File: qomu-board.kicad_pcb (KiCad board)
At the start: 6 copper layers, 28.1 x 10.7 mm, 67 parts, among them IC1 EOS-S3, J1 FTSH-105-01-L-DV-K, J2 825437-4, J3 MC-HVT1-S02-G, Q1 RV1C002UN, Q2 RV1C002UN, Q3 RV1C002UN, SW2 Captouch Pads, U1 MIC5504-3.3YMT, U10 UHD1110-FKA, U2 MIC5504-3.3YMT, U4 GD25Q16CEIGR, U5 MC3635, U9 USB-B

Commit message: Update Kicad design file
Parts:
- added N3: ql_logo, qomu-board-footprints:Ql_logo_mid_9mm, F.Cu at (21.4, 22.3)
- N2: footprint qomu-board-footprints:antmicro-logo_midlayer -> qomu-board-footprints:antmicro-logo_midlayer_4mm
- U4: value GD25Q16CEIGR -> GD25Q16C; footprint qomu-board:GD25Q16CEIGR -> qomu-board-footprints:GD25Q16CEIGR
- moved N2 14.7 mm to (37.1, 21.6), turned to 0 degrees
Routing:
- net GND: track 53.4 -> 51.3 mm
- net +3V3: track 57.9 -> 58.5 mm
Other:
- board size 28.1 x 10.7 mm -> 28.1 x 10.6 mm
- board text added: "qomu"
- board text added: "rev.1.1"
- board text added: "v.1.1"
- board text removed: "Qomu"
- board text removed: "rev.1.0"

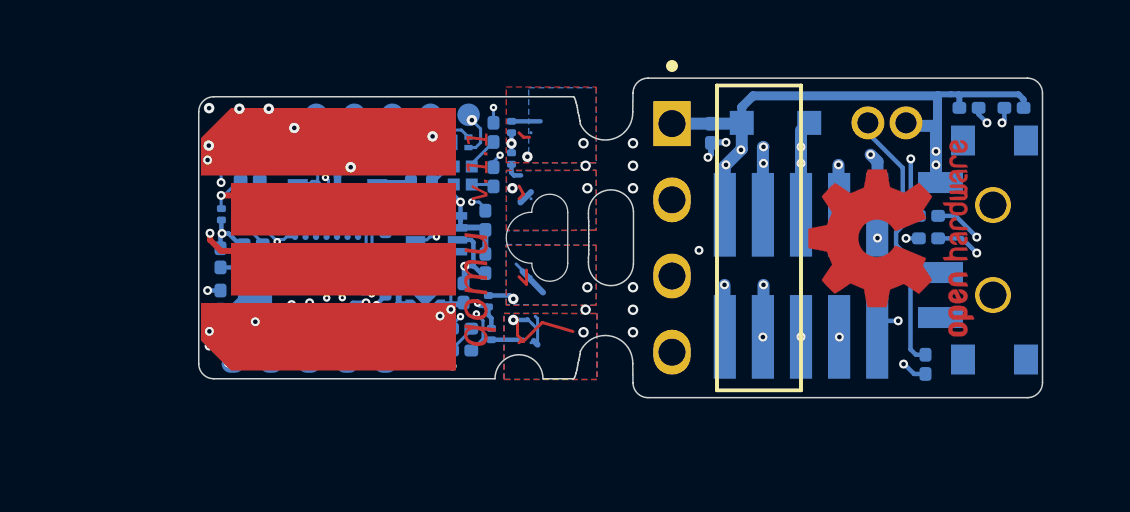
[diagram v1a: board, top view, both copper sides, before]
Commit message: Schematic Update: 1. Remove accel sensor and related passive components 2. Add QL to title Layout Update: 1. Remove accel sensor and related passive components 2. Remove stranded nets: I2C SCL, I2C SDA, IMU_INT, 3,3V, GND
Remains: check stranded via for 3.3V and GND
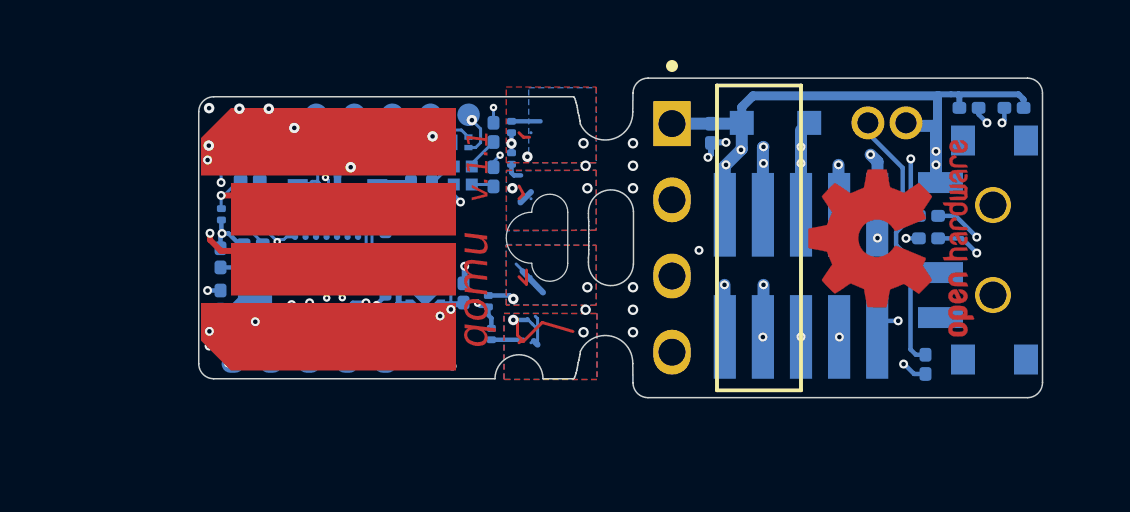
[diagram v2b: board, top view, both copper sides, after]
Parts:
- removed C4: 100n, qomu-board-footprints:C_0201_0603Metric
- removed R3, R4, R8: 4k7, qomu-board-footprints:R_0201_0603Metric
- removed U5: MC3635, qomu-board:MC3635
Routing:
- net /I2C_SDA: track 8.33 -> 0.00 mm, vias 3 -> 0
- net /ACC_INT: track 6.43 -> 0.00 mm, vias 3 -> 0
- net /I2C_SCL: track 5.84 -> 0.00 mm, vias 3 -> 0
- net +3V3: track 58.5 -> 53.6 mm
- net GND: track 51.3 -> 48.0 mm

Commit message: pcb: first attempt at new component placement
There's still a huge ratsnest, but component placement should roughly be
finalized.

Signed-off-by: Sean Cross <sean@xobs.io>
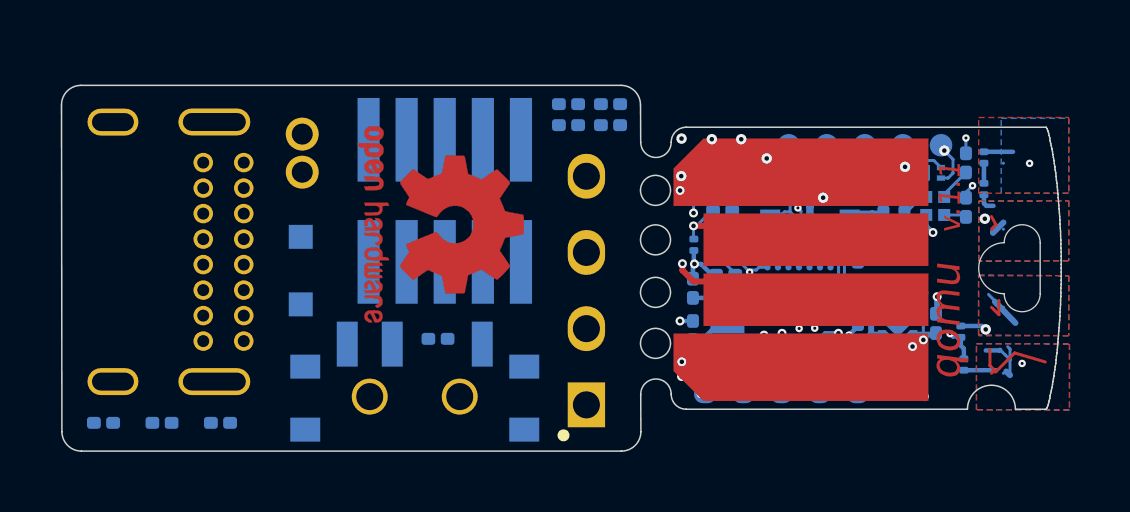
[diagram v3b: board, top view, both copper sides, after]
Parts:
- added J4: USB-C, qomu-board-footprints:USB4085-GF-A, B.Cu at (14.5, 22.3)
- added R3: 5.1k, 1%, 0201, qomu-board-footprints:R_0201_0603Metric, B.Cu at (15.8, 28.0)
- added R4: 5.1k, 1%, 0201, qomu-board-footprints:R_0201_0603Metric, B.Cu at (13.8, 28.0)
- C1, C2, C7, C9: value 2u2/10V -> 2u2, 10V, X5R, 0201
- C10, C11, C12, C3, C5, C6, C8: value 100n -> 100n, 6.3V, X5R, 0201
- C13, C14: value 8p -> 8p, 25V, NP0, 0201
- R1, R13, R15, R2, R5, R6: value 10k -> 10k, 1%, 0201
- R10, R7: value 0R -> 0R, 0201
- R11, R12: value 22R -> 22R, 1%, 0201
- R16, R17: value 100R -> 100R, 1%, 0201
- R18: value 220R -> 220R, 1%, 0201
- R9: value 1k5 -> 1k5, 1%, 0201
- U4: value GD25Q16C -> GD25Q16CEIGR
- moved R6 23.6 mm to (17.8, 28.0), turned to 180 degrees
- moved N2 22.5 mm to (14.7, 23.0)
- moved J3 20.1 mm to (20.5, 18.3), turned to 270 degrees
- moved S1 19.9 mm to (24.2, 27.1), turned to 180 degrees
- moved D8 16.6 mm to (20.4, 22.9), turned to 270 degrees
- moved C1 15.8 mm to (34.2, 25.9)
- moved C7 15.8 mm to (38.6, 25.5)
- moved R2 15.8 mm to (38.6, 26.2)
- moved TP9 15.8 mm to (37.7, 27.0)
- moved U4 15.8 mm to (37.4, 20.8)
- moved XTAL1 15.8 mm to (34.6, 24.3)
- moved C3 15.8 mm to (34.6, 23.0)
- moved C6 15.8 mm to (37.2, 26.2)
- moved C9 15.8 mm to (37.2, 25.5)
- moved D1 15.8 mm to (43.2, 19.1)
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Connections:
- IC1 pad A2: Net-(IC1-PadA2) -> (no net)
- IC1 pad A3: Net-(IC1-PadA3) -> (no net)
- IC1 pad A7: /I2C_SCL -> (no net)
- IC1 pad B2: Net-(IC1-PadB2) -> (no net)
- IC1 pad B7: /I2C_SDA -> (no net)
- IC1 pad C7: /ACC_INT -> (no net)
- IC1 pad D1: Net-(IC1-PadD1) -> (no net)
- J1 pad 7: Net-(J1-Pad7) -> (no net)
- S1 pad 3: Net-(S1-Pad3) -> (no net)
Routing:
- net /SWD_IO: track 31.9 -> 0.00 mm, vias 3 -> 1
- net /RST_N: track 32.4 -> 1.48 mm, vias 6 -> 2
- net +3V3: track 53.6 -> 27.9 mm, vias 28 -> 18
- net /UART_RX: track 26.0 -> 1.01 mm, vias 2 -> 1
- net /C1: track 27.9 -> 4.36 mm, vias 6 -> 4
- net /UART_TX: track 24.6 -> 3.16 mm, vias 3 -> 1
- net /SWD_CLK: track 31.1 -> 13.1 mm, vias 4 -> 7
- net GND: track 48.0 -> 30.7 mm, vias 57 -> 44
- net /LED_G: track 13.3 -> 0.49 mm, vias 8 -> 2
- net Net-(J3-Pad2): track 10.1 -> 0.00 mm
- net /TOUCH_4: track 12.0 -> 2.41 mm
- net Net-(J1-Pad6): track 8.82 -> 0.00 mm, vias 2 -> 0
- net /TOUCH_1: track 14.4 -> 6.18 mm
- net /R_USB_N: track 3.39 -> 11.5 mm, vias 2 -> 4
- net Net-(J1-Pad8): track 7.24 -> 0.00 mm, vias 2 -> 0
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- removed copper zone on In2.Cu, net GND
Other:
- board size 28.1 x 10.6 mm -> 33.3 x 12.2 mm
- board text removed: "1"

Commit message: pcb: re-layout board with new design rules
This lays out the board according to the design rules set forth by the
factory.
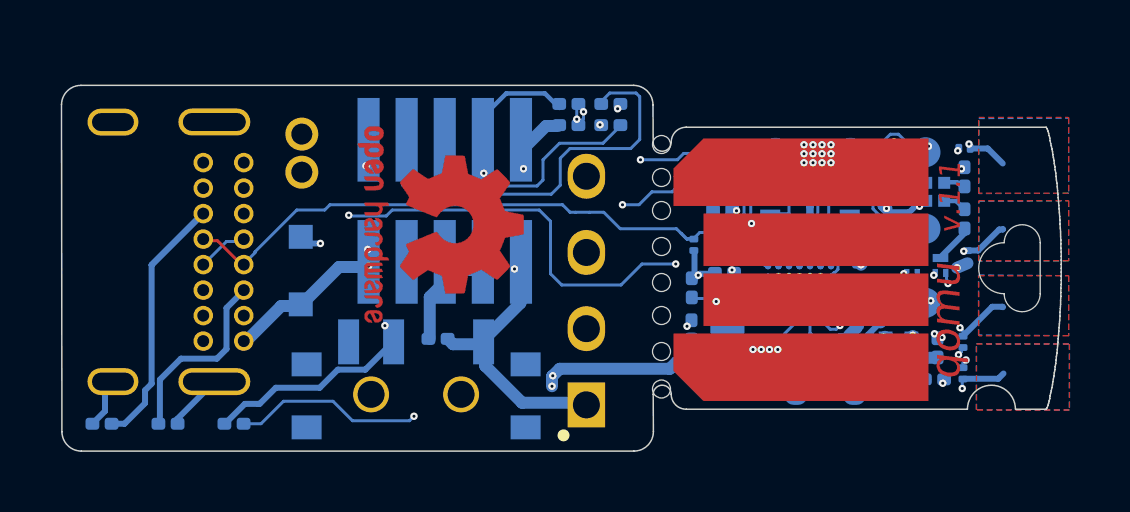
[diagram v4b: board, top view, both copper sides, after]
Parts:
- removed the IC1 at (37.0, 23.7)
- removed TP10, TP2: TP_SMD_0_75MM, qomu-board-footprints:Testpoint_smd_0_75_0_6mm
- removed TP8: TP_SMD_0_75MM, qomu-board-footprints:Testpoint_smd_0_75mm
- added IC1 (x2): EOS-S3, qomu-board:42-WLCSP, B.Cu at (37.0, 23.6)
- added REF**: Castellated_Via, qomu-board-footprints:Castellated_Via, F.Cu at (32.5, 21.6)
- added REF**: Castellated_Via, qomu-board-footprints:Castellated_Via, F.Cu at (32.5, 20.5)
- added REF**: Castellated_Via, qomu-board-footprints:Castellated_Via, F.Cu at (32.5, 22.7)
- added REF**: Castellated_Via, qomu-board-footprints:Castellated_Via, F.Cu at (32.5, 25.1)
- added REF**: Castellated_Via, qomu-board-footprints:Castellated_Via, F.Cu at (32.5, 23.9)
- added REF**: Castellated_Via, qomu-board-footprints:Castellated_Via, F.Cu at (32.5, 26.2)
- added REF**: Castellated_Via, qomu-board-footprints:Castellated_Via, F.Cu at (32.5, 27.4)
- added REF**: Castellated_Via, qomu-board-footprints:Castellated_Via, F.Cu at (32.5, 28.6)
- TP1: footprint qomu-board-footprints:Testpoint_smd_0_75_0_6mm -> qomu-board-footprints:Testpoint_pad_1mm
- TP4, TP5, TP6, TP7: footprint qomu-board-footprints:Testpoint_smd_0_75mm -> qomu-board-footprints:Testpoint_pad_1mm
- moved Q1 8.59 mm to (41.8, 22.8), turned to 90 degrees
- moved TP1 7.93 mm to (41.2, 24.0)
- moved Q2 6.89 mm to (40.8, 22.8), turned to 90 degrees
- moved N3 3.78 mm to (25.2, 22.5)
- moved TP6 3.48 mm to (41.2, 21.5)
- moved D3 2.31 mm to (42.6, 22.4), turned to 270 degrees
- moved R4 2.15 mm to (16.0, 28.0)
- moved R3 2.00 mm to (13.8, 28.0), turned to 0 degrees
- moved Q3 1.68 mm to (40.0, 19.0)
- moved R5 1.44 mm to (41.5, 26.5), turned to 0 degrees
- moved TP9 1.16 mm to (38.9, 27.0)
- moved TP5 0.85 mm to (38.8, 19.0)
- moved C2 0.82 mm to (41.6, 25.5)
- moved TP4 0.80 mm to (41.2, 18.9)
- moved N2 0.75 mm to (14.6, 22.3)
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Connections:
- J4 pad P2: (no net) -> GND
- J4 pad P3: (no net) -> GND
- J4 pad P4: (no net) -> GND
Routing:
- net GND: track 30.7 -> 133.5 mm, vias 44 -> 77
- net +3V3: track 27.9 -> 86.7 mm, vias 18 -> 36
- net +VBUS: track 5.40 -> 50.0 mm, vias 3 -> 27
- net /RST_N: track 1.48 -> 37.2 mm, vias 2 -> 5
- net /USB_P: track 6.28 -> 40.0 mm, vias 1 -> 3
- net /UART_TX: track 3.16 -> 25.8 mm, vias 1 -> 4
- net /C1: track 4.36 -> 24.9 mm, vias 4 -> 6
- net /UART_RX: track 1.01 -> 19.6 mm, vias 1 -> 4
- net /SWD_IO: track 0.00 -> 17.9 mm, vias 1 -> 2
- net /USB_N: track 8.19 -> 25.5 mm, vias 2 -> 4
- net /E1: track 15.0 -> 0.00 mm, vias 4 -> 0
- net Net-(J3-Pad2): track 0.00 -> 12.9 mm, vias 0 -> 1
- net Net-(J1-Pad8): track 0.00 -> 12.6 mm
- net /F2: track 11.7 -> 0.00 mm, vias 2 -> 0
- net /TOUCH_4: track 2.41 -> 13.6 mm, vias 4 -> 6
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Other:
- outline, holes or cut-outs redrawn
- board text added: "In2.Cu: 3.3V"
- board text added: "In3.Cu: GND Plane"

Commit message: pcb: fix routing and drc errors
This fixes all unconnected nets and DRC warnings/errors, and is ready
for fabrication.

Signed-off-by: Sean Cross <sean@xobs.io>
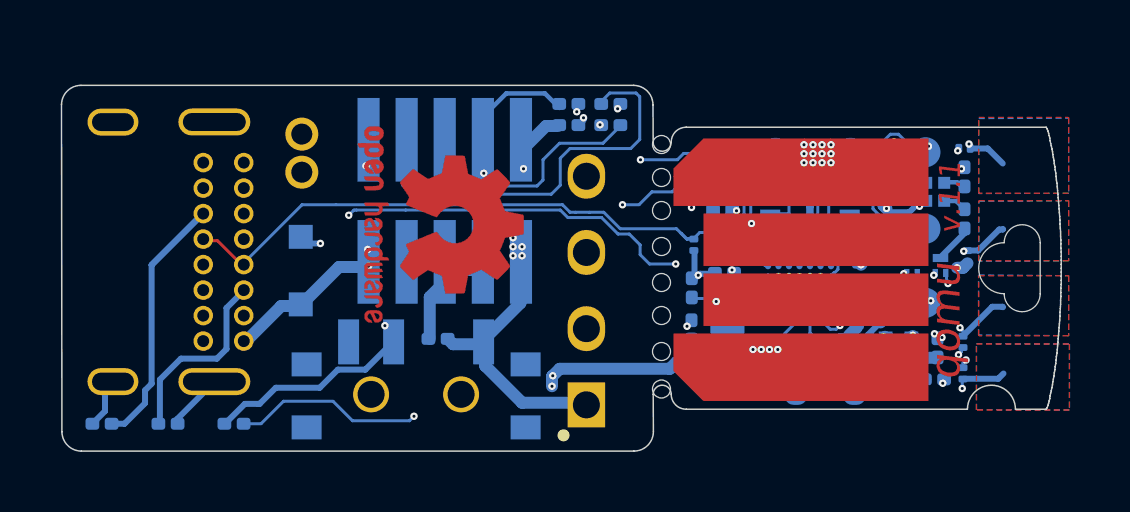
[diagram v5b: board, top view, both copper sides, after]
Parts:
- removed the IC1 at (37.0, 23.6)
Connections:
- IC1 pad A2: Net-(IC1-PadA2) -> (no net)
- IC1 pad A3: Net-(IC1-PadA3) -> (no net)
- IC1 pad B2: Net-(IC1-PadB2) -> (no net)
- IC1 pad B7: Net-(IC1-PadB7) -> (no net)
- IC1 pad C7: Net-(IC1-PadC7) -> (no net)
- IC1 pad D3: Net-(IC1-PadD3) -> (no net)
- IC1 pad E1: Net-(IC1-PadE1) -> (no net)
- IC1 pad F2: Net-(IC1-PadF2) -> (no net)
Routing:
- net GND: track 133.5 -> 143.5 mm
- net +3V3: track 86.7 -> 95.2 mm, vias 36 -> 45
- net +VBUS: track 50.0 -> 55.1 mm
- net /RST_N: track 37.2 -> 35.8 mm
- net /USB_N: track 25.5 -> 25.8 mm, vias 4 -> 5
- net Net-(IC1-PadD3): vias 1 -> 0
- added copper zone on In3.Cu, net +3V3
- added copper zone on In4.Cu, net +3V3
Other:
- rule trace_min: 0.0762 -> 0
- board text removed: "F"
- board text removed: "R"

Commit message: pcb: fix touchpads on backside
The touchpads didn't extend to the backside.

Signed-off-by: Sean Cross <sean@xobs.io>
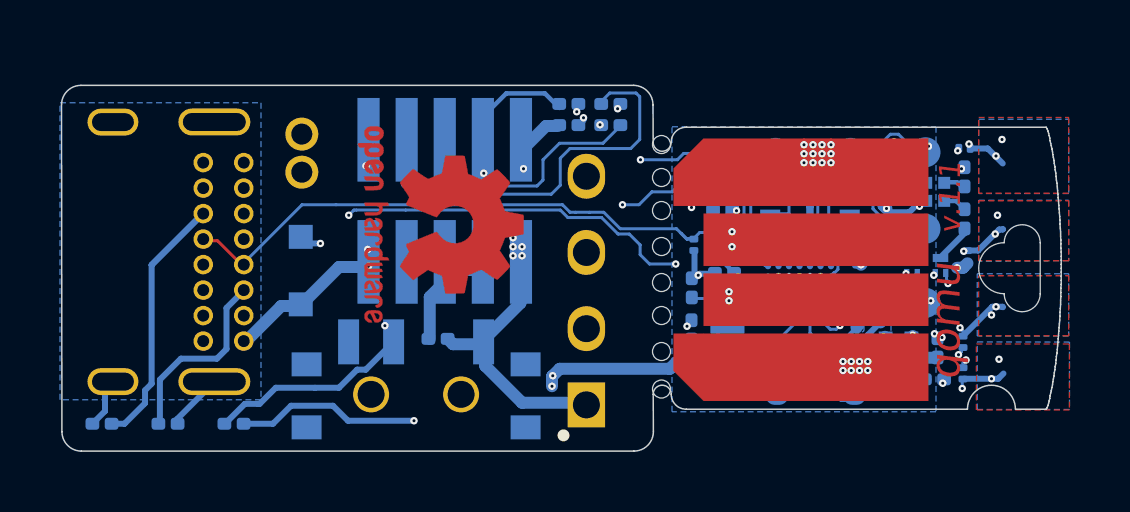
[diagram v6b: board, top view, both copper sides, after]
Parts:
- moved TP3 0.63 mm to (36.3, 27.0)
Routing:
- net GND: track 143.5 -> 156.3 mm, vias 77 -> 82
- net /C1: track 24.9 -> 30.0 mm
- net +3V3: track 95.2 -> 99.3 mm, vias 45 -> 46
- net +VBUS: track 55.1 -> 58.8 mm, vias 27 -> 31
- net /USB_N: track 25.8 -> 28.9 mm, vias 5 -> 7
- net /TOUCH_1: track 8.81 -> 10.5 mm, vias 2 -> 7
- net /TOUCH_3: track 7.03 -> 8.65 mm, vias 2 -> 7
- net /TOUCH_2: track 12.5 -> 14.0 mm, vias 4 -> 9
- net /TOUCH_4: track 13.6 -> 15.1 mm, vias 6 -> 11
- net (no net): track 0.00 -> 0.54 mm
- net /USB_P: track 40.0 -> 40.5 mm, vias 3 -> 5
- added copper zone on B.Cu, net /VCCIOB
- added copper zone on B.Cu, net GND
- added copper zone on In1.Cu, net GND
- added copper zone on In2.Cu, net GND
- added copper zone on In4.Cu, net GND

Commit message: pcb: redo layout in 4-layers
Remove two of the layers, since they were mostly empty anyway.

Signed-off-by: Sean Cross <sean@xobs.io>
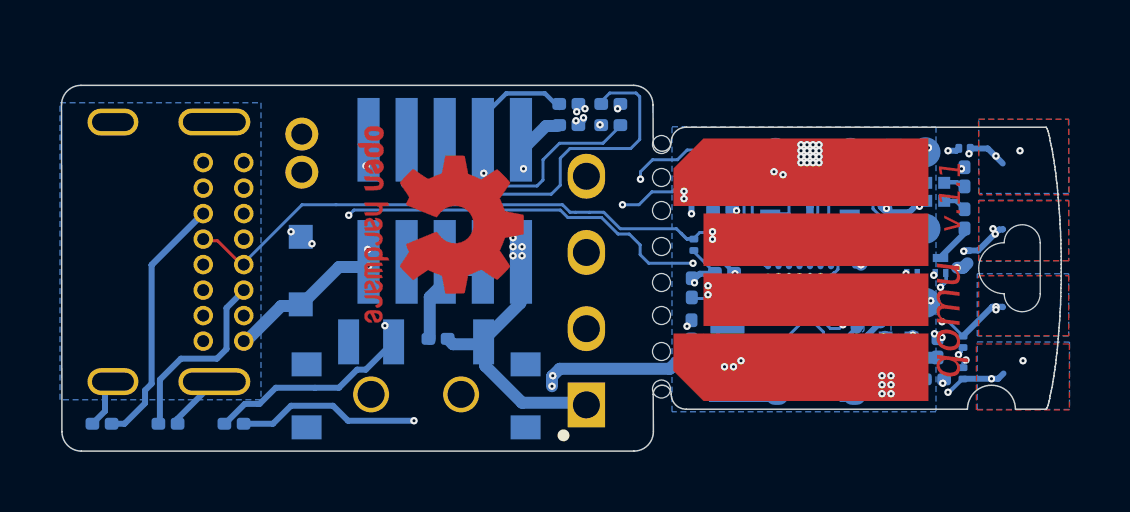
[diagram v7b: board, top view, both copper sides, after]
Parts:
- moved N3 16.8 mm to (38.2, 33.0)
- moved N2 13.0 mm to (22.2, 32.8)
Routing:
- net +3V3: track 99.3 -> 85.5 mm, vias 46 -> 40
- net GND: track 156.3 -> 148.4 mm, vias 82 -> 80
- net +VBUS: track 58.8 -> 53.8 mm, vias 31 -> 24
- net /USB_N: track 28.9 -> 25.6 mm, vias 7 -> 4
- net /USB_P: track 40.5 -> 43.5 mm
- net /TOUCH_2: track 14.0 -> 11.9 mm, vias 9 -> 7
- net Net-(J3-Pad2): track 13.0 -> 14.4 mm
- net /UART_RX: track 19.6 -> 20.4 mm
- net /SPI_SS: track 6.47 -> 5.72 mm
- net (no net): track 0.54 -> 0.00 mm
- net /TOUCH_4: track 15.1 -> 15.6 mm, vias 11 -> 7
- net /TOUCH_3: track 8.65 -> 8.20 mm, vias 7 -> 5
- net /TOUCH_1: track 10.5 -> 10.8 mm, vias 7 -> 5
- net /VCCIOB: track 6.01 -> 5.72 mm, vias 2 -> 0
- added copper zone on In1.Cu, net +3V3
- added copper zone on In1.Cu, net +VBUS
- added copper zone on In1.Cu, net /TOUCH_1
- added copper zone on In2.Cu, net /TOUCH_1
- added copper zone on In1.Cu, net /TOUCH_2
- added copper zone on In2.Cu, net /TOUCH_2
- added copper zone on In1.Cu, net /TOUCH_3
- added copper zone on In2.Cu, net /TOUCH_3
- added copper zone on In1.Cu, net /TOUCH_4
- added copper zone on In2.Cu, net /TOUCH_4
- removed copper zone on In3.Cu, net +3V3
- removed copper zone on In4.Cu, net +3V3
- removed copper zone on In3.Cu, net GND
- removed copper zone on In4.Cu, net GND
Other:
- copper layers 6 -> 4
- board text removed: "rev.1.1"
